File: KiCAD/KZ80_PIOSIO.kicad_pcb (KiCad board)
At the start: 2 copper layers, 100 x 75 mm, 31 parts, among them J1 CON-A, J2 CON-B, J3 PIO-A, J4 PIO-B, J5 SBC8080 BUS, J6 Conn_01x02, J7 ADDR-JP, J8 Z80 CONTROL, Q1 2SC1815, U1 Z80-SIO2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

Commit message: CTC IEOをNC化 & プリントパターン見直し
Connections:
- U4 pad 11: GND -> Net-(U4-Pad11)
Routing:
- net VCC: track 294.2 -> 355.8 mm, vias 0 -> 1
- net PIO-CE: track 108.0 -> 168.4 mm
- net TxDA: track 124.9 -> 69.9 mm
- net RTSA: track 114.6 -> 64.9 mm, vias 0 -> 2
- net RxDB: track 75.4 -> 112.0 mm, vias 0 -> 1
- net /D6: track 135.4 -> 99.8 mm, vias 1 -> 0
- net /D1: track 187.2 -> 164.9 mm
- net A5: track 78.4 -> 58.6 mm, vias 0 -> 1
- net A7: track 68.9 -> 51.7 mm
- net ~INT-J: track 105.0 -> 121.9 mm
- net A0: track 109.3 -> 125.0 mm, vias 2 -> 1
- net /D7: track 112.4 -> 98.5 mm
- net /D0: track 150.7 -> 137.7 mm
- net A6: track 68.6 -> 56.0 mm
- net Net-(U2-Pad22): track 42.7 -> 30.6 mm
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
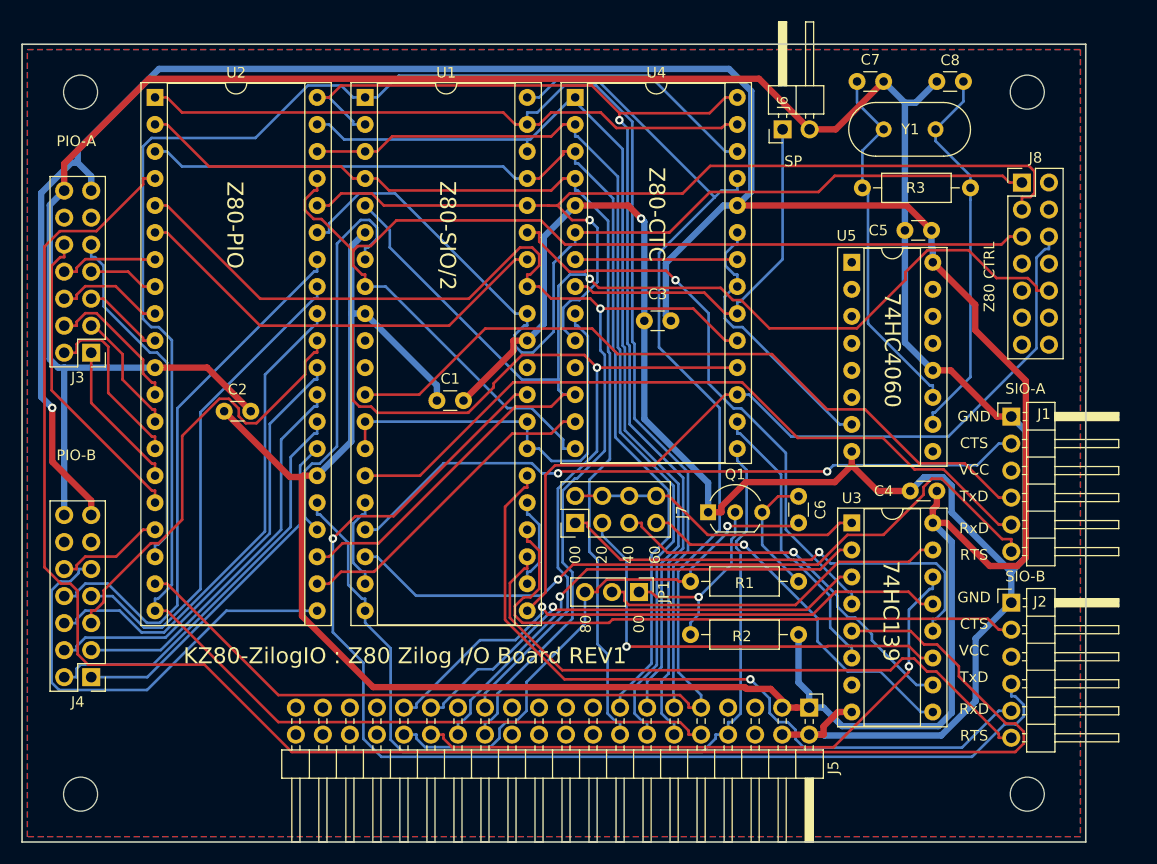
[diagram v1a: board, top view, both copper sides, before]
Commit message: 電源部に電解コンデンサ追加
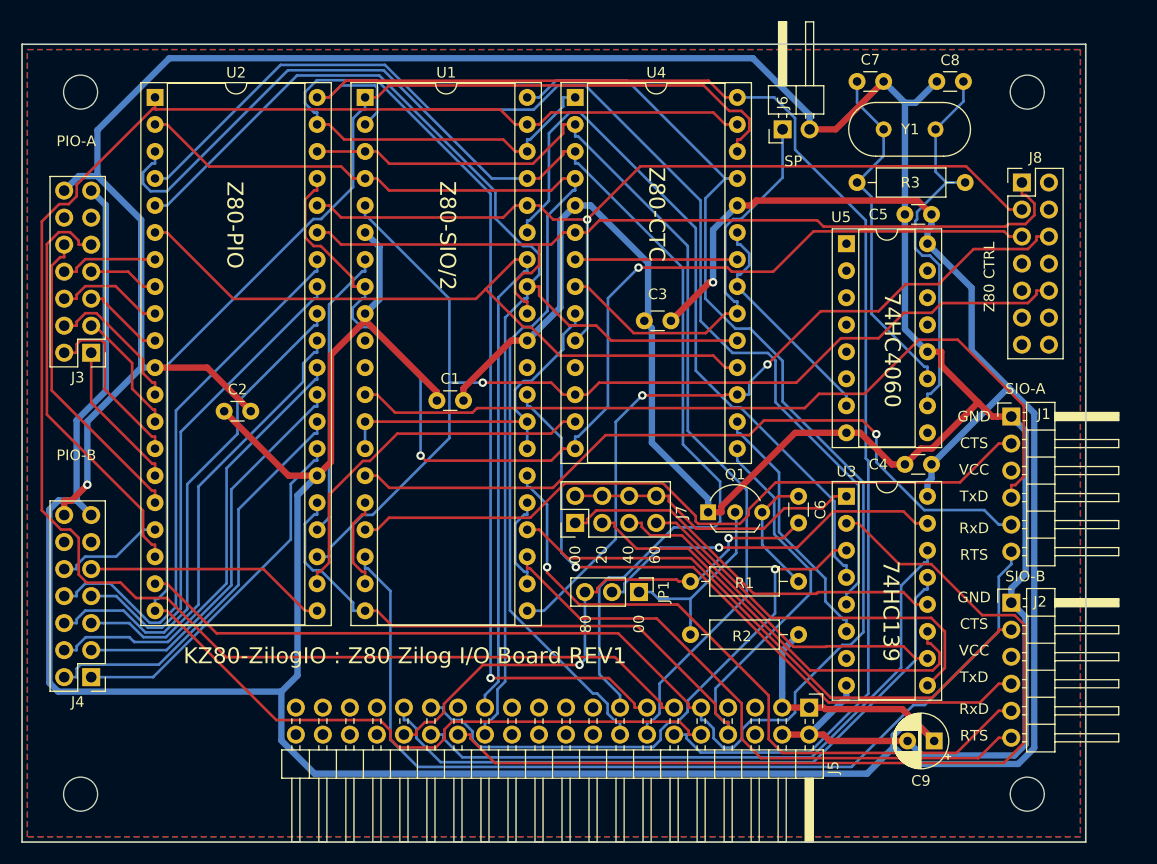
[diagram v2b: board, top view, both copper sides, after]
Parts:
- added C9: 10u, Capacitor_THT:CP_Radial_D5.0mm_P2.50mm, F.Cu at (185.8, 105.5)
- moved C4 2.55 mm to (185.5, 79.5)
- moved U3 2.55 mm to (177.5, 82.5)
- moved U5 1.82 mm to (177.5, 58.8)
- moved C5 1.50 mm to (185.5, 56.0)
- moved R3 0.71 mm to (178.5, 53.0)
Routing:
- net PIO-CE: track 168.4 -> 109.5 mm
- net RxDB: track 112.0 -> 65.2 mm
- net /D2: track 128.3 -> 169.5 mm
- net A3: track 46.5 -> 87.1 mm, vias 1 -> 0
- net /D3: track 109.8 -> 135.6 mm, vias 1 -> 0
- net /D4: track 90.4 -> 116.2 mm, vias 0 -> 1
- net /D6: track 99.8 -> 121.4 mm
- net CTSA: track 70.8 -> 89.8 mm, vias 1 -> 0
- net BRDY: track 41.8 -> 22.9 mm
- net ~INT-J: track 121.9 -> 103.9 mm
- net /D0: track 137.7 -> 155.1 mm
- net A0: track 125.0 -> 109.8 mm, vias 1 -> 0
- net SIO-CE: track 54.3 -> 68.7 mm, vias 1 -> 0
- net Net-(U1-Pad7): track 37.7 -> 27.4 mm
- net ~IORQ: track 92.2 -> 83.3 mm
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
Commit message: 一部回路見直し&回路図出力
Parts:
- added JP2: SIO_JP, Connector_PinHeader_2.54mm:PinHeader_1x03_P2.54mm_Vertical, F.Cu at (172.5, 58.9)
- J6: value Conn_01x02 -> SPK_JP
- J8: footprint Connector_PinHeader_2.54mm:PinHeader_2x07_P2.54mm_Vertical -> Connector_PinHeader_2.54mm:PinHeader_2x07_P2.54mm_Horizontal
- moved J8 2.09 mm to (192.0, 52.3)
- moved J3 0.94 mm to (106.4, 69.9)
- moved J4 0.12 mm to (106.4, 99.5)
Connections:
- net SPK renamed Net-(J6-Pad1)
- U4 pad 9: SIO-CLK -> Net-(JP2-Pad1)
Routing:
- net VCC: track 351.6 -> 0.00 mm, vias 1 -> 0
- net GND: track 335.2 -> 0.00 mm, vias 1 -> 0
- net /D2: track 169.5 -> 0.00 mm
- net /D1: track 158.2 -> 0.00 mm
- net /D0: track 155.1 -> 0.00 mm
- net /D3: track 135.6 -> 0.00 mm
- net /D6: track 121.4 -> 0.00 mm
- net A1: track 119.6 -> 0.00 mm
- net /D4: track 116.2 -> 0.00 mm, vias 1 -> 0
- net A0: track 109.8 -> 0.00 mm
- net PIO-CE: track 109.5 -> 0.00 mm
- net ~M1: track 106.6 -> 0.00 mm, vias 2 -> 0
- net ~INT-J: track 103.9 -> 0.00 mm, vias 1 -> 0
- net /D7: track 102.7 -> 0.00 mm
- net /D5: track 95.1 -> 0.00 mm
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- removed copper zone on B.Cu, net GND
- removed copper zone on F.Cu, net GND
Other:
- board text added: "4060"
- board text added: "CTC"
- board text added: "SPK"
- board text removed: "SP"

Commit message: パターン原点設定、ガーバーデータ再出力
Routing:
- net GND: track 0.00 -> 327.0 mm, vias 0 -> 2
- net VCC: track 0.00 -> 326.4 mm, vias 0 -> 1
- net /D0: track 0.00 -> 162.7 mm
- net /D1: track 0.00 -> 158.1 mm
- net /D2: track 0.00 -> 136.5 mm
- net /D3: track 0.00 -> 122.6 mm
- net A0: track 0.00 -> 119.3 mm, vias 0 -> 1
- net /D7: track 0.00 -> 118.2 mm, vias 0 -> 1
- net A1: track 0.00 -> 117.6 mm, vias 0 -> 1
- net /D4: track 0.00 -> 104.5 mm
- net ~INT-J: track 0.00 -> 103.6 mm
- net RxDB: track 0.00 -> 101.7 mm
- net /D6: track 0.00 -> 97.7 mm
- net ~M1: track 0.00 -> 94.4 mm
- net /D5: track 0.00 -> 93.7 mm, vias 0 -> 1
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- added copper zone on B.Cu, net GND
- added copper zone on F.Cu, net GND
